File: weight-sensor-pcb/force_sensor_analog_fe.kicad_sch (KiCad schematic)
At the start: 34 parts, among them IC1 INA333AIDGKR, IC2 INA333AIDGKR, IC3 INA333AIDGKR, IC4 INA333AIDGKR, J1 Conn_01x04_Socket, J2 Conn_01x04_Socket, J3 Conn_01x04_Socket, J4 Conn_01x04_Socket, U1 OPA333xxD, U2 OPA333xxD, U3 OPA333xxD, U4 OPA333xxD

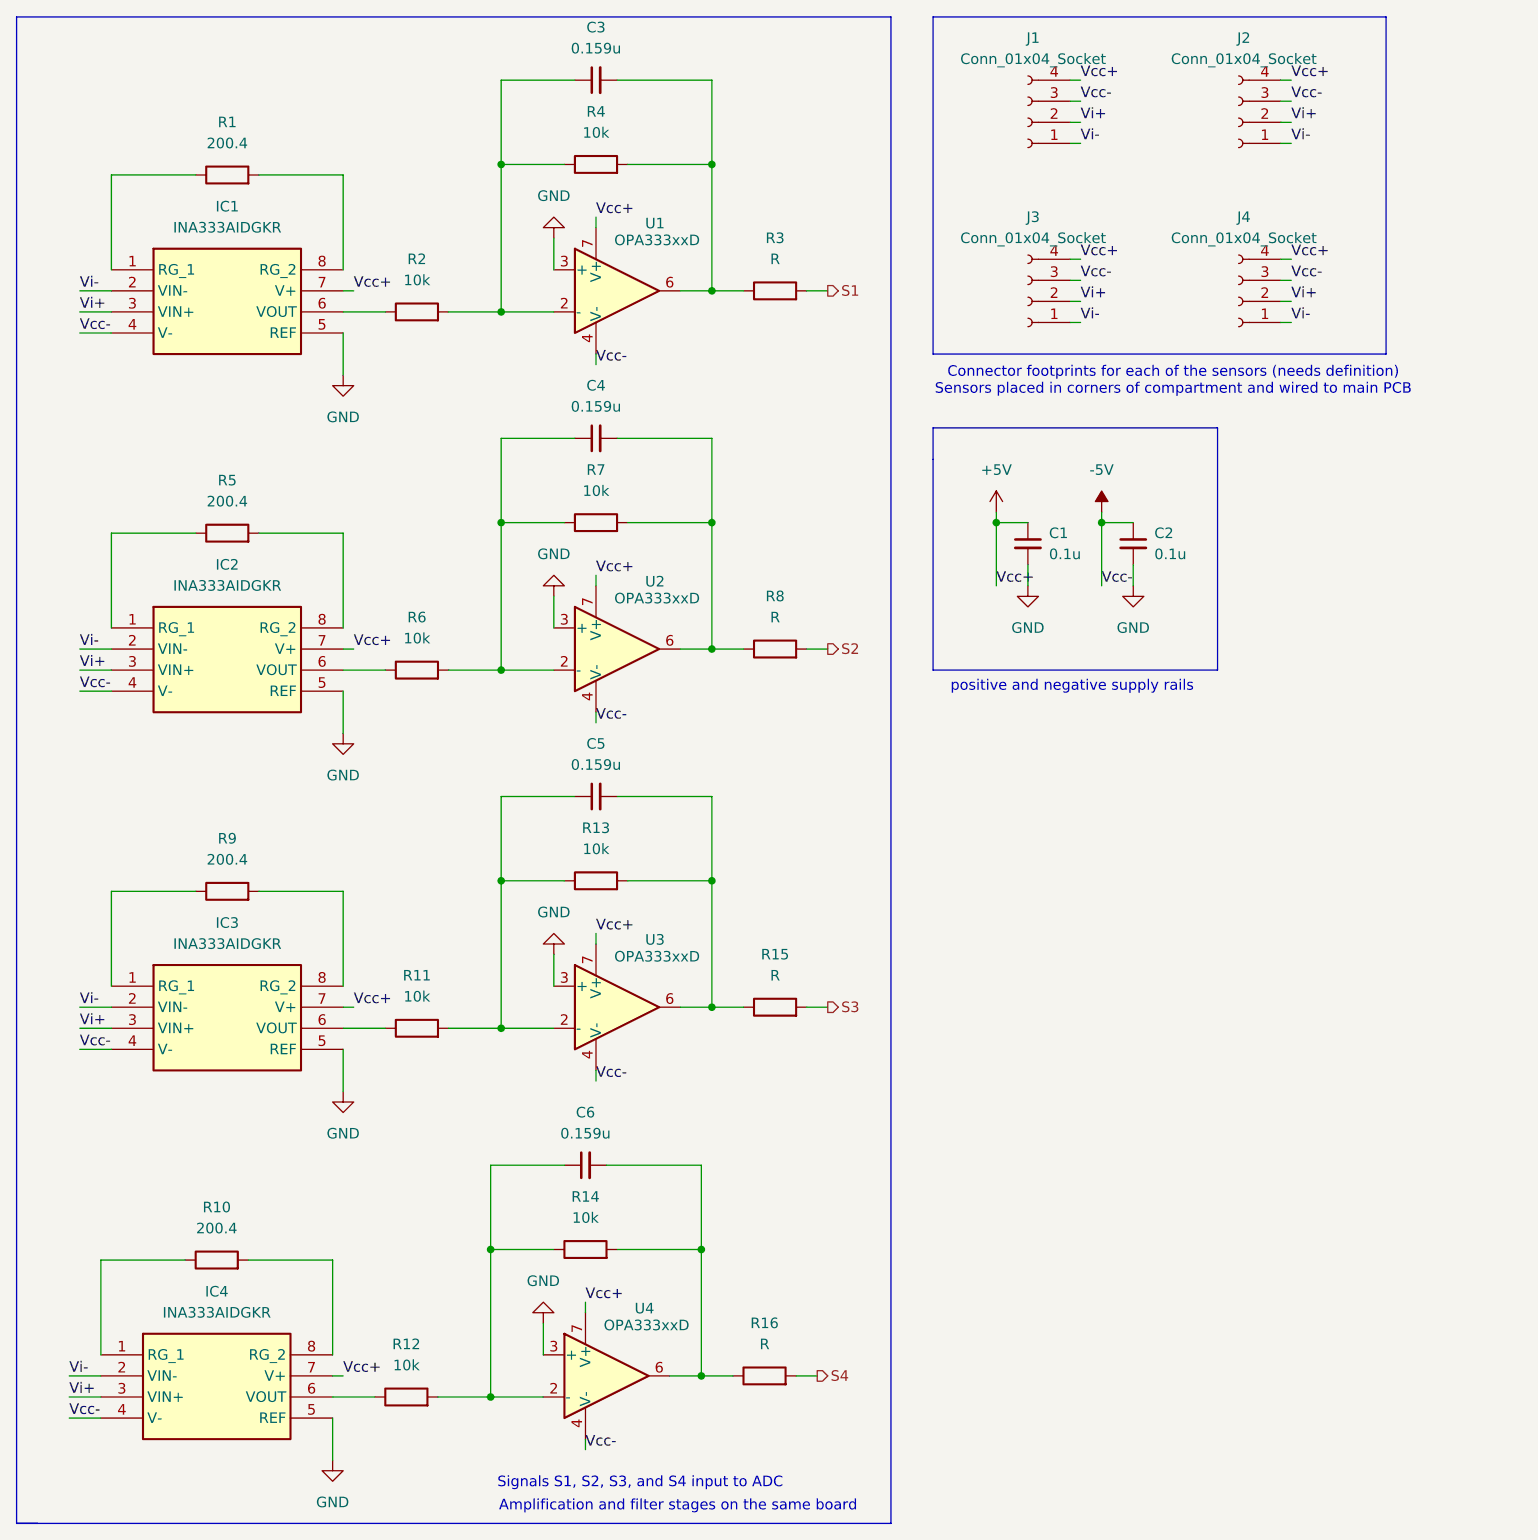
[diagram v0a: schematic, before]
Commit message: update CAN transceiver schematic/layout, use env vars for library paths
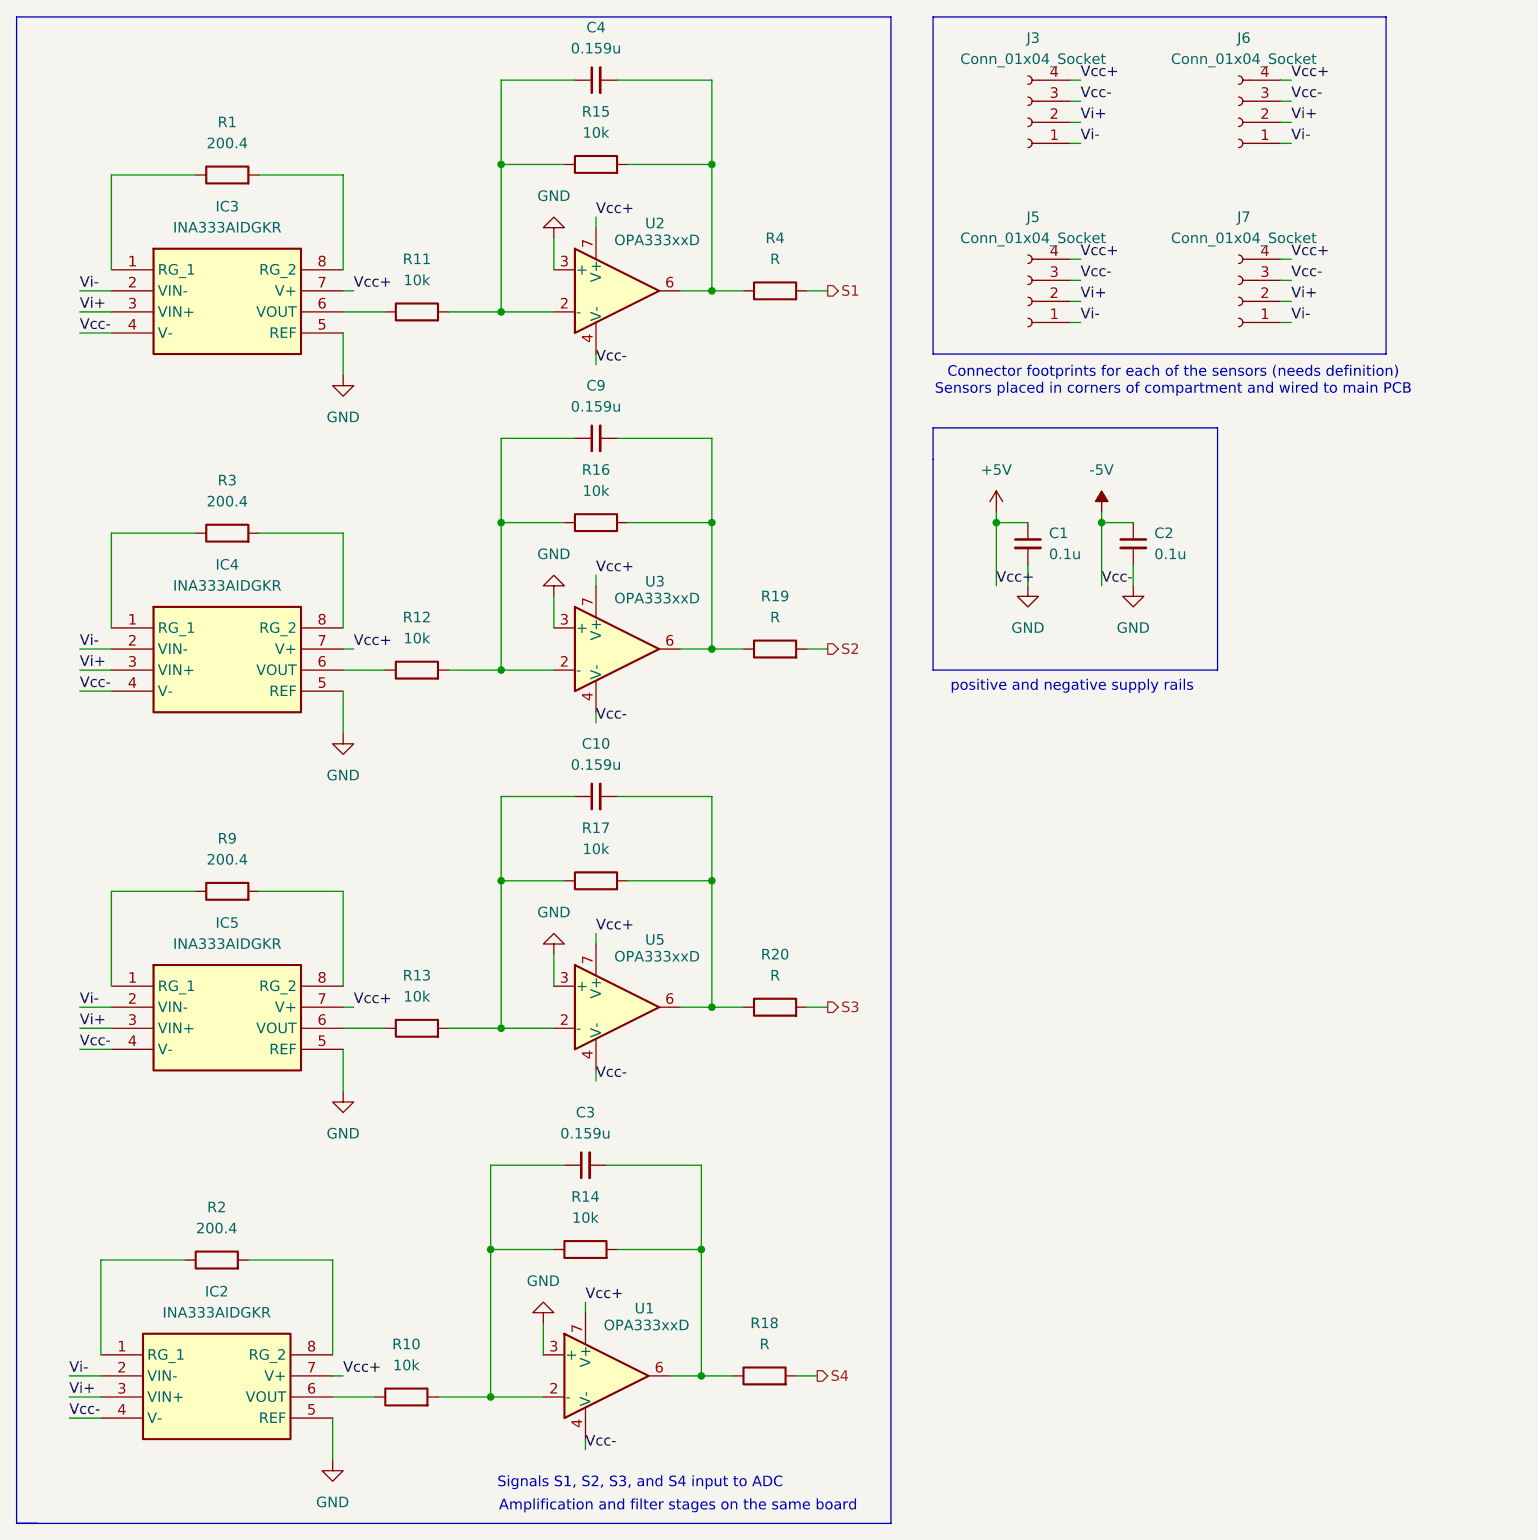
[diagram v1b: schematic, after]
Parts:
- renumbered C5 to C10, C6 to C3, C3 to C4, C4 to C9, IC4 to IC2, IC1 to IC3, IC2 to IC4, IC3 to IC5, J1 to J3, J3 to J5, J2 to J6, J4 to J7, R12 to R10, R2 to R11, R6 to R12, R11 to R13, R4 to R15, R7 to R16, R13 to R17, R16 to R18, R8 to R19, R10 to R2, R15 to R20, R5 to R3, R3 to R4, U4 to U1, U1 to U2, U2 to U3, U3 to U5

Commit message: replace generic components with specific components
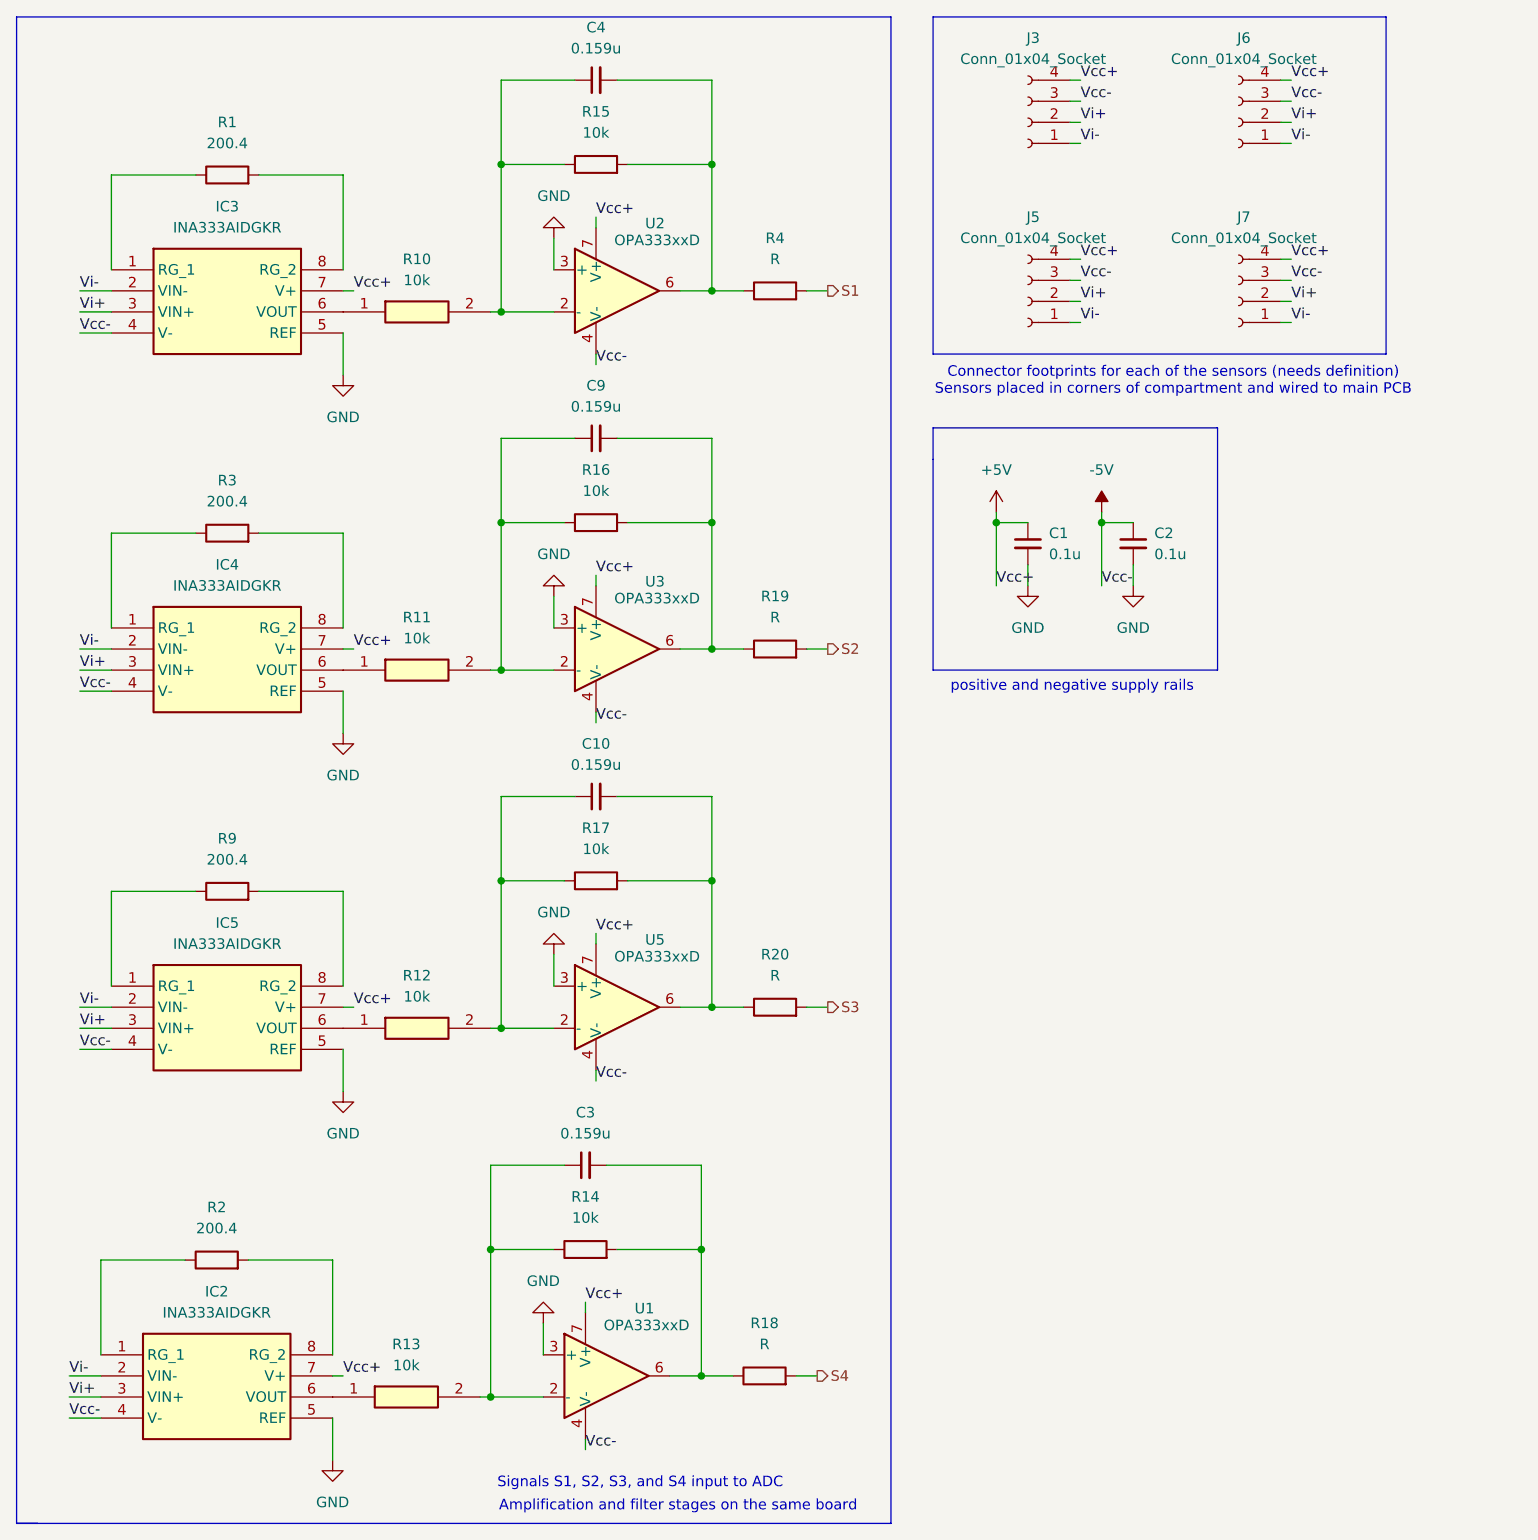
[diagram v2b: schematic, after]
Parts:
- removed R10, R11, R12, R13: 10k, symbol Device:R
- added R10, R11, R12, R13: 10k, RESC1608X55N, symbol Capstone:RMCF0603FT10K0
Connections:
- net at C9.1, R16.1, U3.2 (-): now also R11.2
- net at IC2.6 (VOUT): now also R13.1
- net at C3.1, R14.1, U1.2 (-): now also R13.2
- net at IC4.6 (VOUT): now also R11.1
- net at C4.1, R15.1, U2.2 (-): now also R10.2
- net at IC3.6 (VOUT): now also R10.1
- net at IC5.6 (VOUT): now also R12.1
- net at C10.1, R17.1, U5.2 (-): now also R12.2

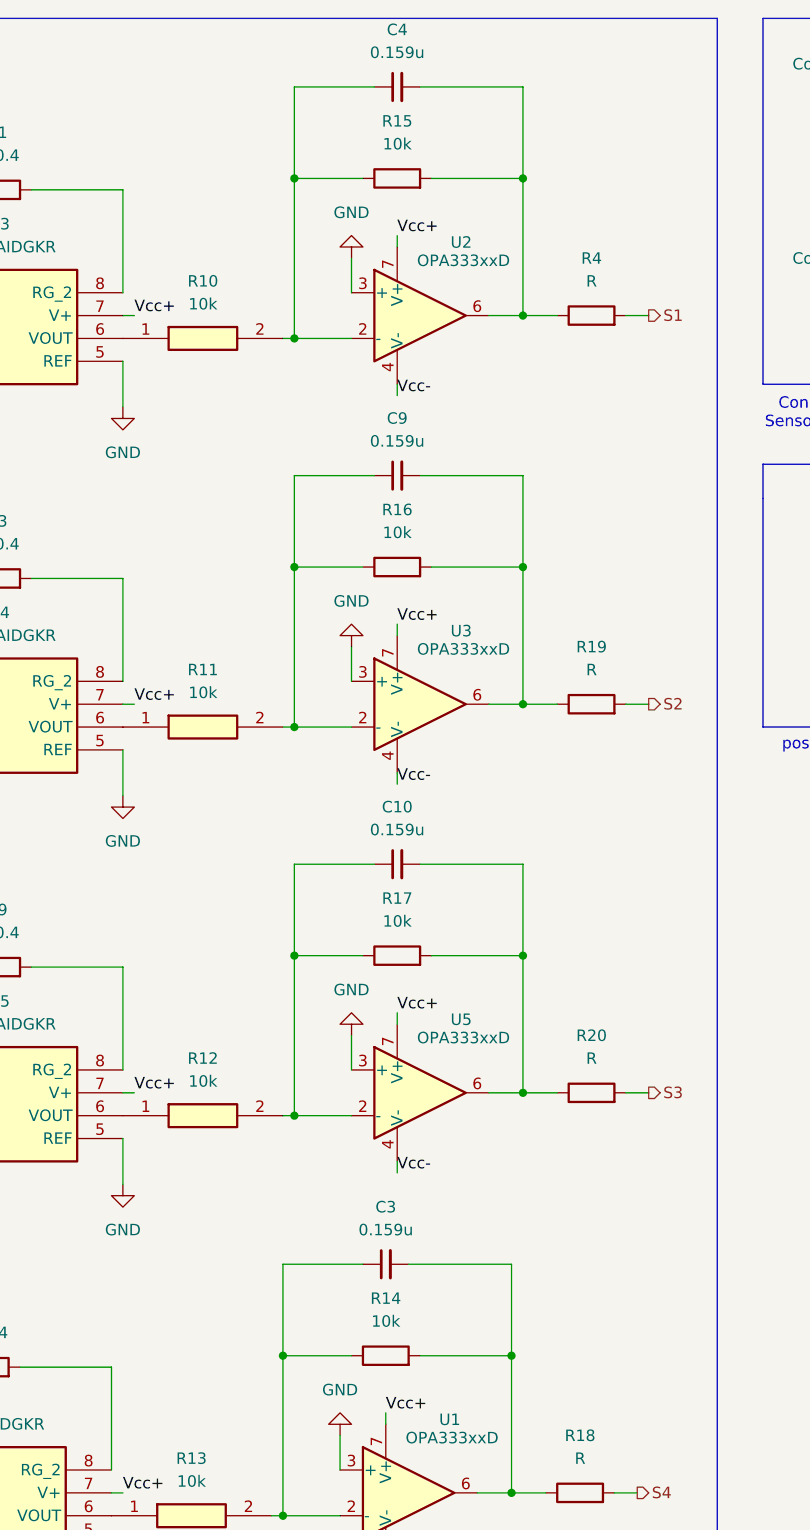
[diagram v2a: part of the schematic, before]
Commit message: replace generic feedback resistors with specific components
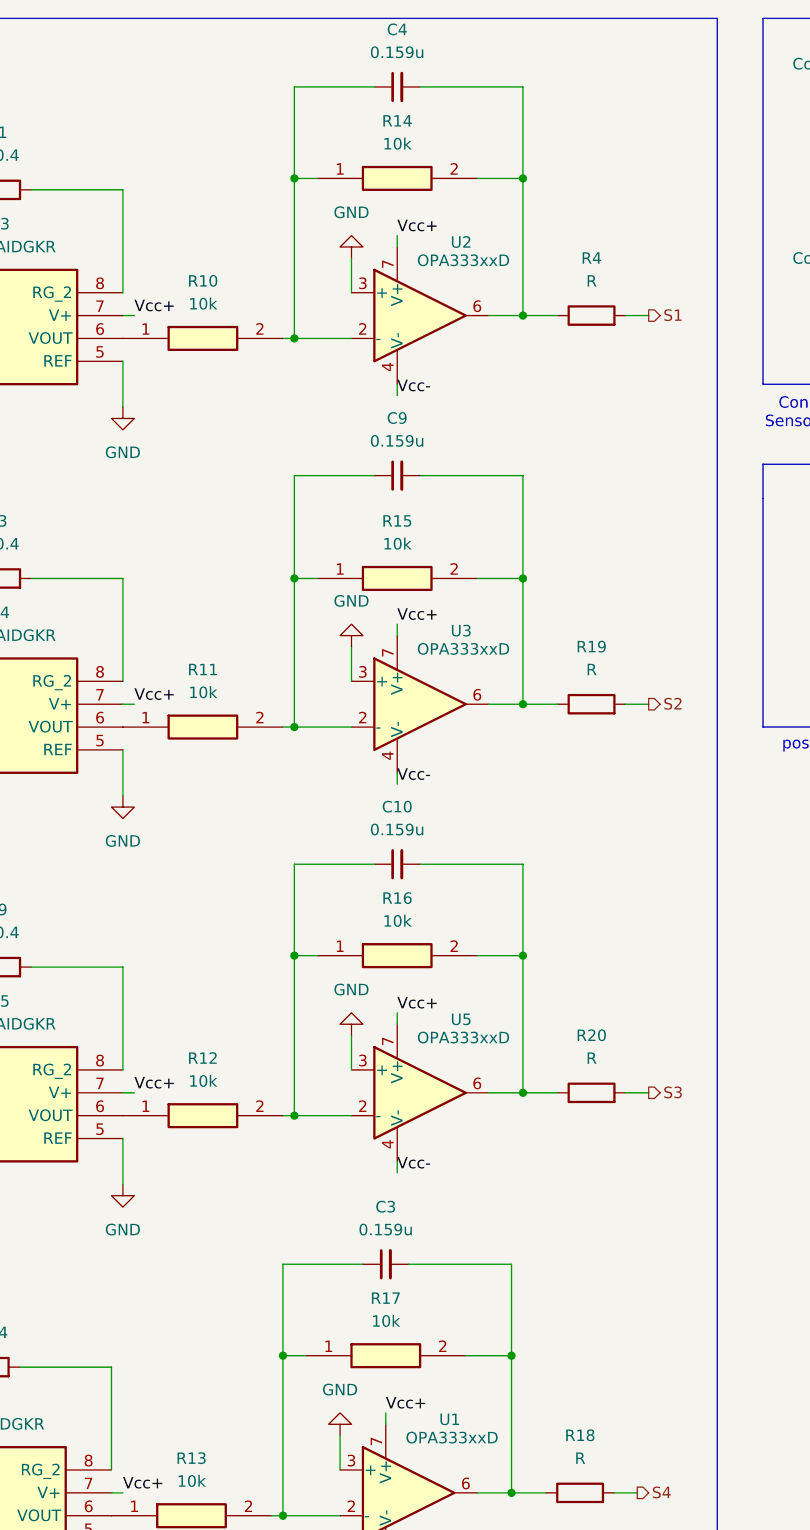
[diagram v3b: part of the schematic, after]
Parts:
- removed R14, R15, R16, R17: 10k, symbol Device:R
- added R14, R15, R16, R17: 10k, RESC1608X55N, symbol Capstone:RMCF0603FT10K0
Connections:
- net at C9.1, R11.2, U3.2 (-): now also R15.1
- net at C9.2, R19.1, U3.6: now also R15.2
- net at C10.2, R20.1, U5.6: now also R16.2
- net at C3.2, R18.1, U1.6: now also R17.2
- net at C4.1, R10.2, U2.2 (-): now also R14.1
- net at C4.2, R4.1, U2.6: now also R14.2
- net at C10.1, R12.2, U5.2 (-): now also R16.1
- net at C3.1, R13.2, U1.2 (-): now also R17.1
